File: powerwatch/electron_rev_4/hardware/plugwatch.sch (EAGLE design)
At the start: 121 parts, among them J1 DM3AT-SF-PEJM5, U1 BGA725L6-ALT, U10 SIP32510, U12 SIP32510, U13 AB1815-T3, U16 MAX6746, U2 SAFFB1G56KB0F0A, U3 IRM-03-5V, U4 MAX-M8, U5 MAX9910, U6 LIS2DW12, U8 MAX9910, U9 SIP32510, X1 ABS07-32.768KHZ-7-T

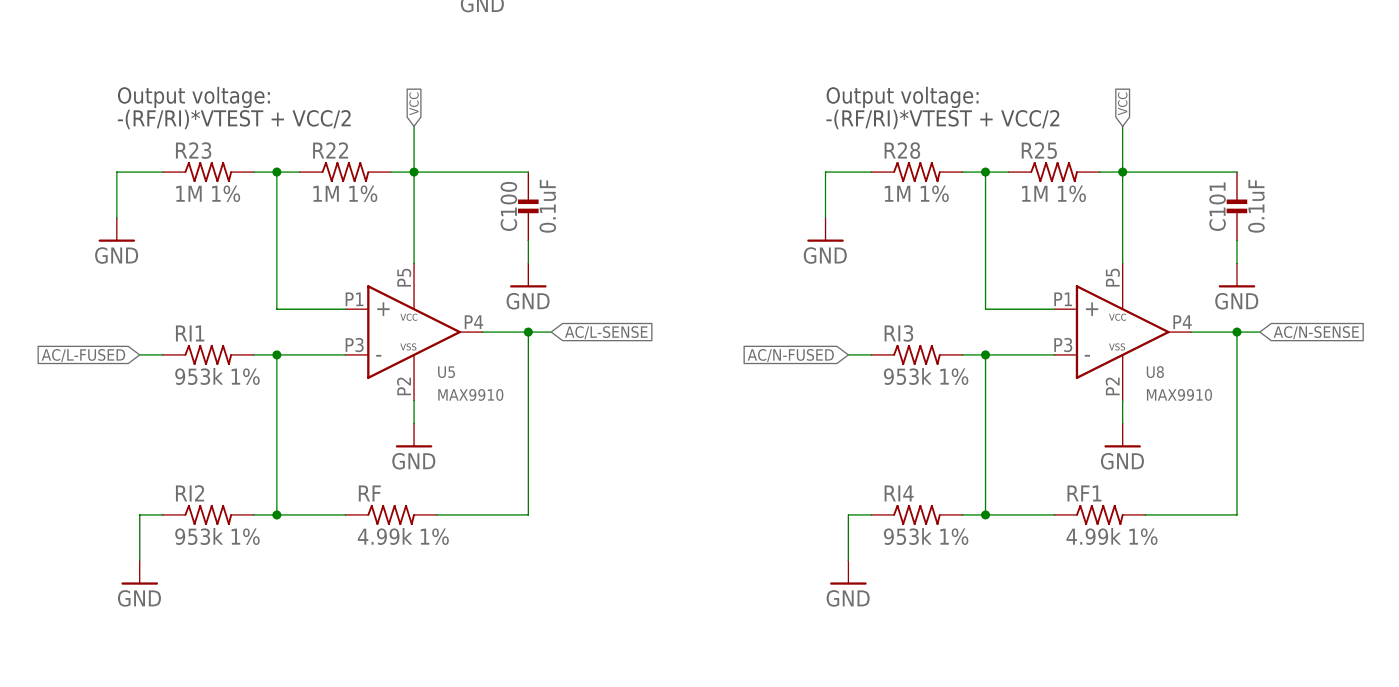
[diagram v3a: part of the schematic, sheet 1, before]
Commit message: almost finished routing - still need to do debug signals
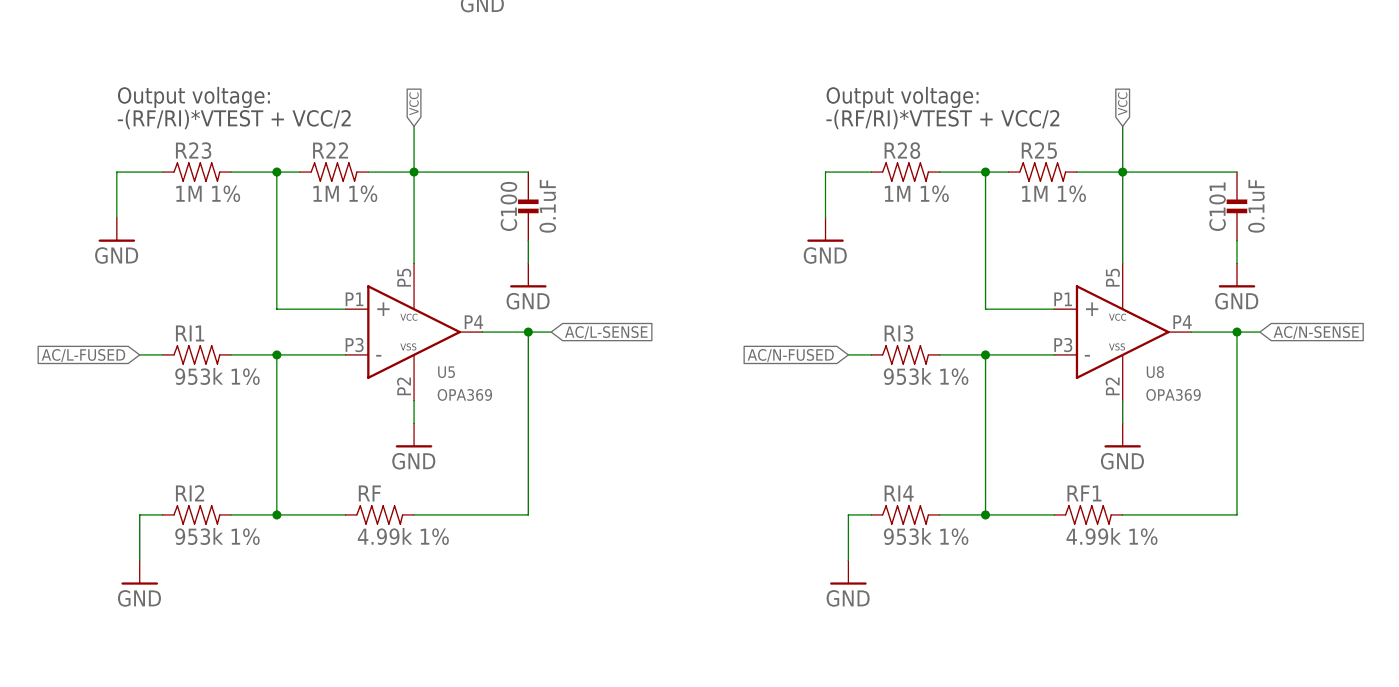
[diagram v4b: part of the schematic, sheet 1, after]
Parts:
- C100, C101: device passives:CAPACITOR0603_CAP -> passives:CAPACITOR0402_CAP
- J1: value DM3AT-SF-PEJM5 -> CON_MICRO_SDDM3AT-SF-PEJM5; device connector:DM3AT-SF-PEJM5 -> connector:CON_MICRO_SDDM3AT-SF-PEJM5
- R21, R30, R31, R8: device passives:RESISTOR0402_RES -> passives:RESISTOR1206_RES_HIGH_CLEARANCE
- R22, R25, RF, RF1, RI2, RI4: device rcl:R-US_R0402 -> passives:RESISTOR0402_RES
- R23, R28: device rcl:R-US_R0402_SM -> passives:RESISTOR0402_RES
- RI1, RI3: device rcl:R-US_R0402 -> passives:RESISTOR1206_RES_HIGH_CLEARANCE
- U5, U8: value MAX9910 -> OPA369; device powerfilm:MAX9910 -> powerfilm:OPA369
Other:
- moved on the sheet: R22, R23, R25, R28, RF, RF1, RI1, RI2, RI3, RI4
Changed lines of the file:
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@@
 <part name="GND35" library="supply1" library_urn="urn:adsk.eagle:library:371" deviceset="GND" device=""/>
 <part name="GND8" library="SparkFun-Aesthetics" deviceset="GND" device=""/>
-<part name="J1" library="connector" deviceset="DM3AT-SF-PEJM5" device=""/>
+<part name="J1" library="connector" deviceset="CON_MICRO_SD" device="DM3AT-SF-PEJM5"/>
 <part name="L1" library="passives" deviceset="INDUCTOR" device="0402" value="5.6nH">
 <attribute name="DESCRIPTION" value="FIXED IND 5.6NH 1.77A 40 MOHM"/>
@@
 <part name="R7" library="varistor" library_urn="urn:adsk.eagle:library:410" deviceset="S14K385" device="" package3d_urn="urn:adsk.eagle:package:30572/1"/>
 <part name="F1" library="powerwatch" deviceset="MICRO_FUSE" device="500MA_350VAC" value="300VAC - 500ma"/>
-<part name="R8" library="passives" deviceset="RESISTOR" device="0402_RES" value="750k">
+<part name="R8" library="passives" deviceset="RESISTOR" device="1206_RES_HIGH_CLEARANCE" value="750k">
 <attribute name="DESCRIPTION" value="RES SMD 150 OHM 1% 1/16W 0402"/>
 <attribute name="DIGIKEY" value="RMCF0402FT150RCT-ND"/>
@@
 </part>
 <part name="SUPPLY2" library="umich" deviceset="GND" device=""/>
-<part name="R21" library="passives" deviceset="RESISTOR" device="0402_RES" value="750k">
-<attribute name="DESCRIPTION" value="RES SMD 150 OHM 1% 1/16W 0402"/>
-<attribute name="DIGIKEY" value="RMCF0402FT150RCT-ND"/>
-<attribute name="MANUFACTURER" value="Stackpole Electronics"/>
-<attribute name="MPN" value="RMCF0402FT150R"/>
-</part>
-<part name="U5" library="powerfilm" deviceset="MAX9910" device="">
+<part name="R21" library="passives" deviceset="RESISTOR" device="1206_RES_HIGH_CLEARANCE" value="750k">
+<attribute name="DESCRIPTION" value="RES SMD 150 OHM 1% 1/16W 0402"/>
+<attribute name="DIGIKEY" value="RMCF0402FT150RCT-ND"/>
+<attribute name="MANUFACTURER" value="Stackpole Electronics"/>
+<attribute name="MPN" value="RMCF0402FT150R"/>
+</part>
+<part name="U5" library="powerfilm" deviceset="OPA369" device="" value="OPA369">
 <attribute name="DIGIKEY" value="296-25252-1-ND"/>
 </part>
-<part name="RF" library="rcl" deviceset="R-US_" device="R0402" value="4.99k 1%">
+<part name="RF" library="passives" deviceset="RESISTOR" device="0402_RES" value="4.99k 1%">
 <attribute name="DIGIKEY" value="P4.99KLCT-ND"/>
 </part>
-<part name="R22" library="rcl" deviceset="R-US_" device="R0402" value="1M 1%">
+<part name="R22" library="passives" deviceset="RESISTOR" device="0402_RES" value="1M 1%">
 <attribute name="DIGIKEY" value="P1.00MLCT-ND"/>
 </part>
-<part name="R23" library="rcl" deviceset="R-US_" device="R0402_SM" value="1M 1%">
+<part name="R23" library="passives" deviceset="RESISTOR" device="0402_RES" value="1M 1%">
 <attribute name="DIGIKEY" value="P1.00MLCT-ND"/>
 </part>
-<part name="RI1" library="rcl" deviceset="R-US_" device="R0402" value="953k 1%">
+<part name="RI1" library="passives" deviceset="RESISTOR" device="1206_RES_HIGH_CLEARANCE" value="953k 1%">
 <attribute name="DIGIKEY" value="P953KLCT-ND"/>
 </part>
-<part name="RI2" library="rcl" deviceset="R-US_" device="R0402" value="953k 1%">
+<part name="RI2" library="passives" deviceset="RESISTOR" device="0402_RES" value="953k 1%">
 <attribute name="DIGIKEY" value="P953KLCT-ND"/>
 </part>
 <part name="SUPPLY3" library="umich" deviceset="GND" device=""/>
-<part name="C100" library="passives" deviceset="CAPACITOR" device="0603_CAP" value="0.1uF"/>
+<part name="C100" library="passives" deviceset="CAPACITOR" device="0402_CAP" value="0.1uF"/>
 <part name="SUPPLY4" library="umich" deviceset="GND" device=""/>
 <part name="SUPPLY5" library="umich" deviceset="GND" device=""/>
 <part name="SUPPLY6" library="umich" deviceset="GND" device=""/>
-<part name="U8" library="powerfilm" deviceset="MAX9910" device="">
+<part name="U8" library="powerfilm" deviceset="OPA369" device="" value="OPA369">
 <attribute name="DIGIKEY" value="296-25252-1-ND"/>
 </part>
-<part name="RF1" library="rcl" deviceset="R-US_" device="R0402" value="4.99k 1%">
+<part name="RF1" library="passives" deviceset="RESISTOR" device="0402_RES" value="4.99k 1%">
 <attribute name="DIGIKEY" value="P4.99KLCT-ND"/>
 </part>
-<part name="R25" library="rcl" deviceset="R-US_" device="R0402" value="1M 1%">
+<part name="R25" library="passives" deviceset="RESISTOR" device="0402_RES" value="1M 1%">
 <attribute name="DIGIKEY" value="P1.00MLCT-ND"/>
 </part>
-<part name="R28" library="rcl" deviceset="R-US_" device="R0402_SM" value="1M 1%">
+<part name="R28" library="passives" deviceset="RESISTOR" device="0402_RES" value="1M 1%">
 <attribute name="DIGIKEY" value="P1.00MLCT-ND"/>
 </part>
-<part name="RI3" library="rcl" deviceset="R-US_" device="R0402" value="953k 1%">
+<part name="RI3" library="passives" deviceset="RESISTOR" device="1206_RES_HIGH_CLEARANCE" value="953k 1%">
 <attribute name="DIGIKEY" value="P953KLCT-ND"/>
 </part>
-<part name="RI4" library="rcl" deviceset="R-US_" device="R0402" value="953k 1%">
+<part name="RI4" library="passives" deviceset="RESISTOR" device="0402_RES" value="953k 1%">
 <attribute name="DIGIKEY" value="P953KLCT-ND"/>
 </part>
 <part name="SUPPLY7" library="umich" deviceset="GND" device=""/>
-<part name="C101" library="passives" deviceset="CAPACITOR" device="0603_CAP" value="0.1uF"/>
+<part name="C101" library="passives" deviceset="CAPACITOR" device="0402_CAP" value="0.1uF"/>
 <part name="SUPPLY8" library="umich" deviceset="GND" device=""/>
 <part name="SUPPLY9" library="umich" deviceset="GND" device=""/>
 <part name="SUPPLY10" library="umich" deviceset="GND" device=""/>
-<part name="R30" library="passives" deviceset="RESISTOR" device="0402_RES" value="750k">
+<part name="R30" library="passives" deviceset="RESISTOR" device="1206_RES_HIGH_CLEARANCE" value="750k">
 <attribute name="DESCRIPTION" value="RES SMD 150 OHM 1% 1/16W 0402"/>
 <attribute name="DIGIKEY" value="RMCF0402FT150RCT-ND"/>
@@
 <attribute name="MPN" value="MM3Z3V3B"/>
 </part>
-<part name="R31" library="passives" deviceset="RESISTOR" device="0402_RES" value="750k">
+<part name="R31" library="passives" deviceset="RESISTOR" device="1206_RES_HIGH_CLEARANCE" value="750k">
 <attribute name="DESCRIPTION" value="RES SMD 150 OHM 1% 1/16W 0402"/>
 <attribute name="DIGIKEY" value="RMCF0402FT150RCT-ND"/>
@@
 <pinref part="R23" gate="G$1" pin="2"/>
 <pinref part="R22" gate="G$1" pin="1"/>
-<wire x1="45.72" y1="78.74" x2="48.26" y2="78.74" width="0.1524" layer="91"/>
+<wire x1="43.18" y1="78.74" x2="48.26" y2="78.74" width="0.1524" layer="91"/>
 <wire x1="48.26" y1="78.74" x2="50.8" y2="78.74" width="0.1524" layer="91"/>
 <wire x1="48.26" y1="78.74" x2="48.26" y2="63.5" width="0.1524" layer="91"/>
@@
 <segment>
 <pinref part="RF1" gate="G$1" pin="2"/>
-<wire x1="144.78" y1="40.64" x2="154.94" y2="40.64" width="0.1524" layer="91"/>
+<wire x1="142.24" y1="40.64" x2="154.94" y2="40.64" width="0.1524" layer="91"/>
 <wire x1="154.94" y1="40.64" x2="154.94" y2="60.96" width="0.1524" layer="91"/>
 <wire x1="157.48" y1="60.96" x2="154.94" y2="60.96" width="0.1524" layer="91"/>
@@
 <segment>
 <pinref part="RI1" gate="G$1" pin="2"/>
-<wire x1="45.72" y1="58.42" x2="48.26" y2="58.42" width="0.1524" layer="91"/>
+<wire x1="43.18" y1="58.42" x2="48.26" y2="58.42" width="0.1524" layer="91"/>
 <wire x1="48.26" y1="58.42" x2="48.26" y2="40.64" width="0.1524" layer="91"/>
 <pinref part="RI2" gate="G$1" pin="2"/>
-<wire x1="48.26" y1="40.64" x2="45.72" y2="40.64" width="0.1524" layer="91"/>
+<wire x1="48.26" y1="40.64" x2="43.18" y2="40.64" width="0.1524" layer="91"/>
 <pinref part="RF" gate="G$1" pin="1"/>
 <wire x1="48.26" y1="40.64" x2="55.88" y2="40.64" width="0.1524" layer="91"/>
@@
 <junction x="63.5" y="78.74"/>
 <pinref part="R22" gate="G$1" pin="2"/>
-<wire x1="63.5" y1="78.74" x2="60.96" y2="78.74" width="0.1524" layer="91"/>
+<wire x1="63.5" y1="78.74" x2="58.42" y2="78.74" width="0.1524" layer="91"/>
 <pinref part="U5" gate="G$1" pin="VCC"/>
 <wire x1="63.5" y1="68.58" x2="63.5" y2="78.74" width="0.1524" layer="91"/>
@@
 <junction x="142.24" y="78.74"/>
 <pinref part="R25" gate="G$1" pin="2"/>
-<wire x1="142.24" y1="78.74" x2="139.7" y2="78.74" width="0.1524" layer="91"/>
+<wire x1="142.24" y1="78.74" x2="137.16" y2="78.74" width="0.1524" layer="91"/>
 <pinref part="U8" gate="G$1" pin="VCC"/>
 <wire x1="142.24" y1="68.58" x2="142.24" y2="78.74" width="0.1524" layer="91"/>
@@
 <pinref part="R28" gate="G$1" pin="2"/>
 <pinref part="R25" gate="G$1" pin="1"/>
-<wire x1="124.46" y1="78.74" x2="127" y2="78.74" width="0.1524" layer="91"/>
+<wire x1="121.92" y1="78.74" x2="127" y2="78.74" width="0.1524" layer="91"/>
 <wire x1="127" y1="78.74" x2="129.54" y2="78.74" width="0.1524" layer="91"/>
 <wire x1="127" y1="78.74" x2="127" y2="63.5" width="0.1524" layer="91"/>
@@
 <segment>
 <pinref part="RI3" gate="G$1" pin="2"/>
-<wire x1="124.46" y1="58.42" x2="127" y2="58.42" width="0.1524" layer="91"/>
+<wire x1="121.92" y1="58.42" x2="127" y2="58.42" width="0.1524" layer="91"/>
 <wire x1="127" y1="58.42" x2="127" y2="40.64" width="0.1524" layer="91"/>
 <pinref part="RI4" gate="G$1" pin="2"/>
-<wire x1="127" y1="40.64" x2="124.46" y2="40.64" width="0.1524" layer="91"/>
+<wire x1="127" y1="40.64" x2="121.92" y2="40.64" width="0.1524" layer="91"/>
 <pinref part="RF1" gate="G$1" pin="1"/>
 <wire x1="127" y1="40.64" x2="134.62" y2="40.64" width="0.1524" layer="91"/>
@@
 <segment>
 <pinref part="RF" gate="G$1" pin="2"/>
-<wire x1="66.04" y1="40.64" x2="76.2" y2="40.64" width="0.1524" layer="91"/>
+<wire x1="63.5" y1="40.64" x2="76.2" y2="40.64" width="0.1524" layer="91"/>
 <wire x1="76.2" y1="40.64" x2="76.2" y2="60.96" width="0.1524" layer="91"/>
 <wire x1="78.74" y1="60.96" x2="76.2" y2="60.96" width="0.1524" layer="91"/>

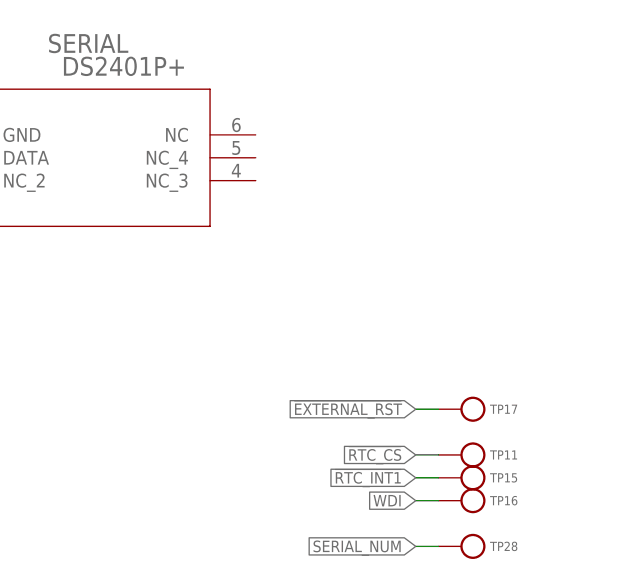
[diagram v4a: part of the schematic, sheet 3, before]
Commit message: layed out debug header, most of the way done routing
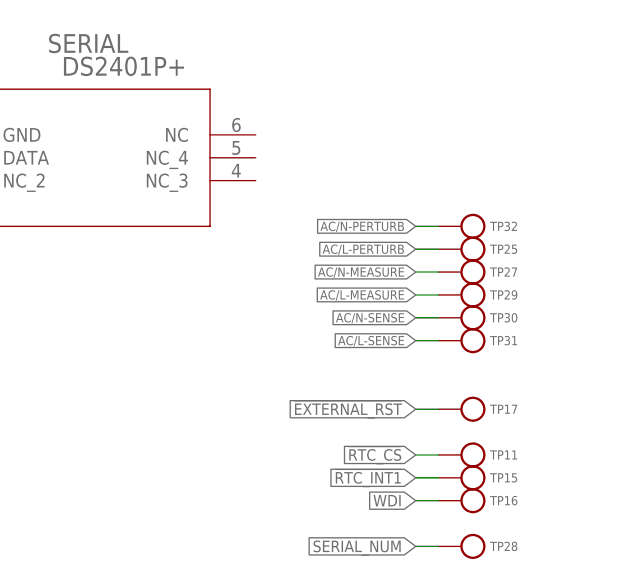
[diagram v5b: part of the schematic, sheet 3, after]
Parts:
- added TP25, TP27, TP29, TP30, TP31, TP32: TEST_POINT_0.040IN, headers:TEST_POINT_0.040IN
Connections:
- net AC/L-MEASURE: now also TP29.TESTPOINT
- net AC/L-PERTURB: now also TP25.TESTPOINT
- net AC/L-SENSE: now also TP31.TESTPOINT
- net AC/N-MEASURE: now also TP27.TESTPOINT
- net AC/N-PERTURB: now also TP32.TESTPOINT
- net AC/N-SENSE: now also TP30.TESTPOINT
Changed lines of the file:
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@@
 <drawing>
 <settings>
-<setting alwaysvectorfont="no"/>
+<setting alwaysvectorfont="yes"/>
 <setting verticaltext="up"/>
 </settings>
@@
 </part>
 <part name="GND4" library="SparkFun-Aesthetics" deviceset="GND" device=""/>
+<part name="TP25" library="headers" deviceset="TEST_POINT_0.040IN" device=""/>
+<part name="TP27" library="headers" deviceset="TEST_POINT_0.040IN" device=""/>
+<part name="TP29" library="headers" deviceset="TEST_POINT_0.040IN" device=""/>
+<part name="TP30" library="headers" deviceset="TEST_POINT_0.040IN" device=""/>
+<part name="TP31" library="headers" deviceset="TEST_POINT_0.040IN" device=""/>
+<part name="TP32" library="headers" deviceset="TEST_POINT_0.040IN" device=""/>
 </parts>
 <sheets>
@@
 <instance part="TP16" gate="G$1" x="236.22" y="101.6" rot="R180"/>
 <instance part="TP17" gate="G$1" x="236.22" y="111.76" rot="R180"/>
+<instance part="TP25" gate="G$1" x="236.22" y="129.54" rot="R180"/>
+<instance part="TP27" gate="G$1" x="236.22" y="127" rot="R180"/>
+<instance part="TP29" gate="G$1" x="236.22" y="124.46" rot="R180"/>
+<instance part="TP30" gate="G$1" x="236.22" y="121.92" rot="R180"/>
+<instance part="TP31" gate="G$1" x="236.22" y="119.38" rot="R180"/>
+<instance part="TP32" gate="G$1" x="236.22" y="132.08" rot="R180"/>
 </instances>
 <busses>
@@
 <label x="60.96" y="109.22" size="1.27" layer="95" rot="R180" xref="yes"/>
 </segment>
+<segment>
+<pinref part="TP30" gate="G$1" pin="TESTPOINT"/>
+<wire x1="233.68" y1="121.92" x2="231.14" y2="121.92" width="0.1524" layer="91"/>
+<label x="231.14" y="121.92" size="1.016" layer="95" rot="R180" xref="yes"/>
+</segment>
 </net>
 <net name="AC/N-MEASURE" class="0">
@@
 <label x="60.96" y="111.76" size="1.27" layer="95" rot="R180" xref="yes"/>
 </segment>
+<segment>
+<pinref part="TP27" gate="G$1" pin="TESTPOINT"/>
+<wire x1="233.68" y1="127" x2="231.14" y2="127" width="0.1524" layer="91"/>
+<label x="231.14" y="127" size="1.016" layer="95" rot="R180" xref="yes"/>
+</segment>
 </net>
 <net name="AC/L-SENSE" class="0">
@@
 <label x="60.96" y="114.3" size="1.27" layer="95" rot="R180" xref="yes"/>
 </segment>
+<segment>
+<pinref part="TP31" gate="G$1" pin="TESTPOINT"/>
+<wire x1="233.68" y1="119.38" x2="231.14" y2="119.38" width="0.1524" layer="91"/>
+<label x="231.14" y="119.38" size="1.016" layer="95" rot="R180" xref="yes"/>
+</segment>
 </net>
 <net name="AC/L-MEASURE" class="0">
@@
 <label x="60.96" y="116.84" size="1.27" layer="95" rot="R180" xref="yes"/>
 </segment>
+<segment>
+<pinref part="TP29" gate="G$1" pin="TESTPOINT"/>
+<wire x1="233.68" y1="124.46" x2="231.14" y2="124.46" width="0.1524" layer="91"/>
+<label x="231.14" y="124.46" size="1.016" layer="95" rot="R180" xref="yes"/>
+</segment>
 </net>
 <net name="AC/L-PERTURB" class="0">
@@
 <label x="60.96" y="119.38" size="1.27" layer="95" rot="R180" xref="yes"/>
 </segment>
+<segment>
+<pinref part="TP25" gate="G$1" pin="TESTPOINT"/>
+<wire x1="233.68" y1="129.54" x2="231.14" y2="129.54" width="0.1524" layer="91"/>
+<label x="231.14" y="129.54" size="1.016" layer="95" rot="R180" xref="yes"/>
+</segment>
 </net>
 <net name="AC/N-PERTURB" class="0">
@@
 <label x="60.96" y="121.92" size="1.27" layer="95" rot="R180" xref="yes"/>
 </segment>
-</net>
+<segment>
+<pinref part="TP32" gate="G$1" pin="TESTPOINT"/>
+<wire x1="233.68" y1="132.08" x2="231.14" y2="132.08" width="0.1524" layer="91"/>
+<label x="231.14" y="132.08" size="1.016" layer="95" rot="R180" xref="yes"/>
+</segment>
+</net>

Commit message: fixed based on case, rerouted, some of the silk
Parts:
- U20: SPICEPREFIX (none) -> X
- renumbered SERIAL to U20
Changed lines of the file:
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@@
 <drawing>
 <settings>
-<setting alwaysvectorfont="yes"/>
+<setting alwaysvectorfont="no"/>
 <setting verticaltext="up"/>
 </settings>
@@
 </part>
 <part name="U9" library="chips" deviceset="SIP32510" device=""/>
-<part name="SERIAL" library="DS2401P+" deviceset="DS2401P+" device=""/>
+<part name="U20" library="DS2401P+" deviceset="DS2401P+" device="">
+<attribute name="SPICEPREFIX" value="X"/>
+</part>
 <part name="P+4" library="supply1" library_urn="urn:adsk.eagle:library:371" deviceset="VCC" device=""/>
 <part name="R29" library="passives" deviceset="RESISTOR" device="0402_RES" value="5K">
@@
 <instance part="TP6" gate="G$1" x="236.22" y="78.74" rot="R180"/>
 <instance part="U12" gate="G$1" x="45.72" y="48.26"/>
-<instance part="SERIAL" gate="A" x="175.26" y="142.24"/>
+<instance part="U20" gate="A" x="175.26" y="142.24"/>
 <instance part="P+4" gate="VCC" x="162.56" y="160.02"/>
 <instance part="R29" gate="G$1" x="162.56" y="149.86" rot="R270">
@@
 </segment>
 <segment>
-<pinref part="SERIAL" gate="A" pin="GND"/>
+<pinref part="U20" gate="A" pin="GND"/>
 <pinref part="GND41" gate="1" pin="GND"/>
 <wire x1="177.8" y1="142.24" x2="170.18" y2="142.24" width="0.1524" layer="91"/>
@@
 </segment>
 <segment>
-<pinref part="SERIAL" gate="A" pin="DATA"/>
+<pinref part="U20" gate="A" pin="DATA"/>
 <wire x1="177.8" y1="139.7" x2="162.56" y2="139.7" width="0.1524" layer="91"/>
 <pinref part="R29" gate="G$1" pin="2"/>
